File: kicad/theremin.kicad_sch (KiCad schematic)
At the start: 40 parts, among them J1 Eurorack Mono Jack, J2 Aerial, SW1 SW_SPDT, U1 4069, U2 4069, U3 LM386, U4 LP2950-5.0_TO92

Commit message: Updating with new footprints and some tweaks
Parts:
- removed D3: 1N4001, Diode_THT:D_DO-35_SOD27_P7.62mm_Horizontal, symbol Diode:1N4148
- removed H2: MountingHole_Pad, MountingHole:MountingHole_3.2mm_M3_DIN965_Pad, symbol Mechanical:MountingHole_Pad
- added D4: 1N4148, Diode_THT:D_DO-35_SOD27_P7.62mm_Horizontal, symbol Diode:1N4148
- added J3: Expression Attachment, Connector_PinHeader_2.54mm:PinHeader_1x02_P2.54mm_Vertical, symbol Connector:Conn_01x02_Pin
- added R12: 270k, Resistor_THT:R_Axial_DIN0207_L6.3mm_D2.5mm_P10.16mm_Horizontal, symbol Device:R
- BT1: footprint Connector_PinHeader_2.54mm:PinHeader_1x02_P2.54mm_Vertical -> Battery:BatteryHolder_Eagle_12BH611-GR
- C1, C2: footprint Rumblesan_Standard_Parts:C_Rect_L7.0mm_W3.5mm_P5.00mm -> Capacitor_THT:C_Rect_L7.0mm_W3.5mm_P5.00mm; Spec (none) -> ceramic C0G; Tolerance (none) -> 1%
- C10, C11, C6, C8, C9: footprint Rumblesan_Standard_Parts:CP_Radial_D5.0mm_P2.00mm -> Capacitor_THT:CP_Radial_D5.0mm_P2.50mm; symbol Rumblesan Standard Parts:C_Polarized -> Device:C_Polarized
- C12: footprint Rumblesan_Standard_Parts:C_Rect_L7.0mm_W3.5mm_P5.00mm -> Capacitor_THT:C_Rect_L7.0mm_W3.5mm_P5.00mm; symbol Rumblesan Standard Parts:C -> Device:C; Spec ceramic C0G -> ceramic X7R
- C3, C4, C5, C7: footprint Rumblesan_Standard_Parts:C_Rect_L7.0mm_W3.5mm_P5.00mm -> Capacitor_THT:C_Rect_L7.0mm_W3.5mm_P5.00mm; symbol Rumblesan Standard Parts:C -> Device:C
- H1: footprint MountingHole:MountingHole_3.2mm_M3_DIN965_Pad -> project-footprints:BCM_Logo_small_Copper_Pad_15mmx15mm; now left out of the parts list
- J2: now left out of the parts list
- LS1: footprint Connector_PinHeader_2.54mm:PinHeader_1x02_P2.54mm_Vertical -> project-footprints:Speaker_PUIAudio_AS04008MR-21-R
- R1, R10, R11, R2, R3, R4, R5, R6, R7, R8, R9: footprint Rumblesan_Standard_Parts:R_Axial_DIN0207_L6.3mm_D2.5mm_P10.16mm_Horizontal -> Resistor_THT:R_Axial_DIN0207_L6.3mm_D2.5mm_P10.16mm_Horizontal; symbol Rumblesan Standard Parts:R -> Device:R
- RV2: value 100k -> 25k; footprint Rumblesan_Standard_Parts:Potentiometer_Alpha_RD901F-40-00D_Single_Vertical -> Potentiometer_THT:Potentiometer_Alpha_RD901F-40-00D_Single_Vertical
- RV3: footprint Rumblesan_Standard_Parts:Potentiometer_Alpha_RD901F-40-00D_Single_Vertical -> Potentiometer_THT:Potentiometer_Alpha_RD901F-40-00D_Single_Vertical
- SW1: footprint Rumblesan_Standard_Parts:SW_SPDT_DailyWell_Sub_MiniToggle -> Button_Switch_THT:SW_CuK_OS102011MA1QN1_SPDT_Angled; MPRN (none) -> OS102011MA1QN1
- U1, U2: footprint Rumblesan_Standard_Parts:DIP-14_W7.62mm_Socket -> Package_DIP:DIP-14_W7.62mm_Socket_LongPads
- U3: footprint Rumblesan_Standard_Parts:DIP-8_W7.62mm_Socket -> Package_DIP:DIP-8_W7.62mm_Socket_LongPads
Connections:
- net GND: now also R11.1, R5.1, R9.1, D4.2 (A), R12.1; no longer R11.2, R5.2, R9.2
- net SPEAKER_AMP: now also R12.2
- net at U1.1: now also R1.1; no longer R1.2
- net at U1.2, U1.3: now also R2.1; no longer R2.2
- net at C5.2, U1.11, U1.13: now also R7.2, R8.2; no longer R7.1, R8.1
- net at U2.10, U2.9: now also C2.1; no longer C2.2
- net at R6.2: now also C4.2, R7.1; no longer C3.2
- net at U2.11, U2.12: now also R4.1; no longer R4.2
- net at U2.13: now also R3.1; no longer R3.2
- net at D1.1 (K), D2.1 (K), U1.9: now also R5.2; no longer R5.1
- net at J1.2 (Tip), RV2.2: now also J3.1 (Pin_1)
- net at U1.4, U1.5: now also C1.1; no longer C1.2
- net at C5.1, C6.1, U1.10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: now also R8.1; no longer R8.2
- net at RV3.3: now also R11.2; no longer R11.1
- net at C11.1, U4.3 (VI): now also R10.2, D4.1 (K); no longer R10.1
- net at RV1.2, RV1.3: now also R4.2; no longer R4.1
- net at C6.2, RV2.1: now also J3.2 (Pin_2)
- net at C7.1: now also R9.2; no longer R9.1
- net at SW1.1 (A): now also R10.1; no longer R10.2
- new net: C1.2, J2.1 (Pin_1), J2.2 (Pin_2), R1.2, R2.2
- new net: C3.2, R6.1
- new net: C2.2, R3.2, RV1.1
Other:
- note added: "BCM Logo with Ground Connection"
- moved on the sheet: BT1, C10, C11, C12, C5, C6, C7, C8, C9, J1, LS1, R10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

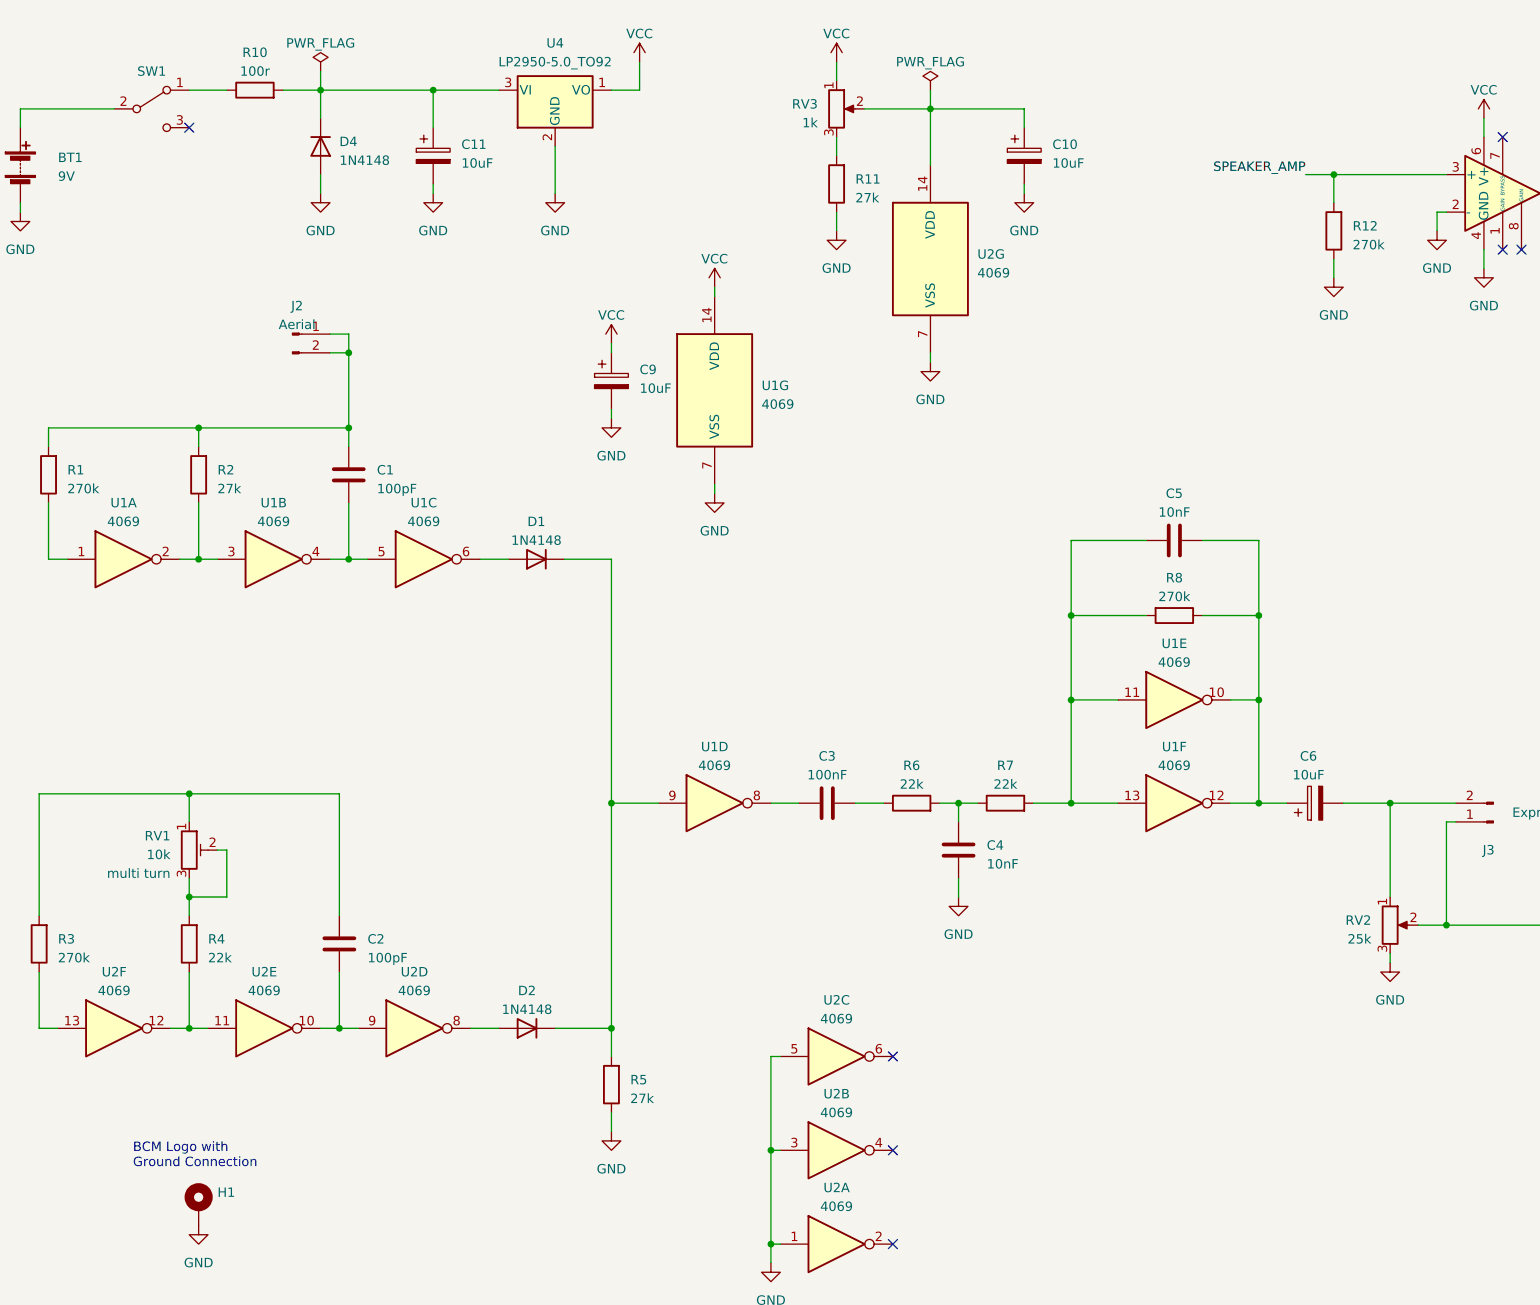
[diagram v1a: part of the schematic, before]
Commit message: Now with extra pretty!
Added the updated prettiefied version of the theremin files and added some quality of life features such as battery clip, crocodile clip friendly connectors, built in speaker & a power switch
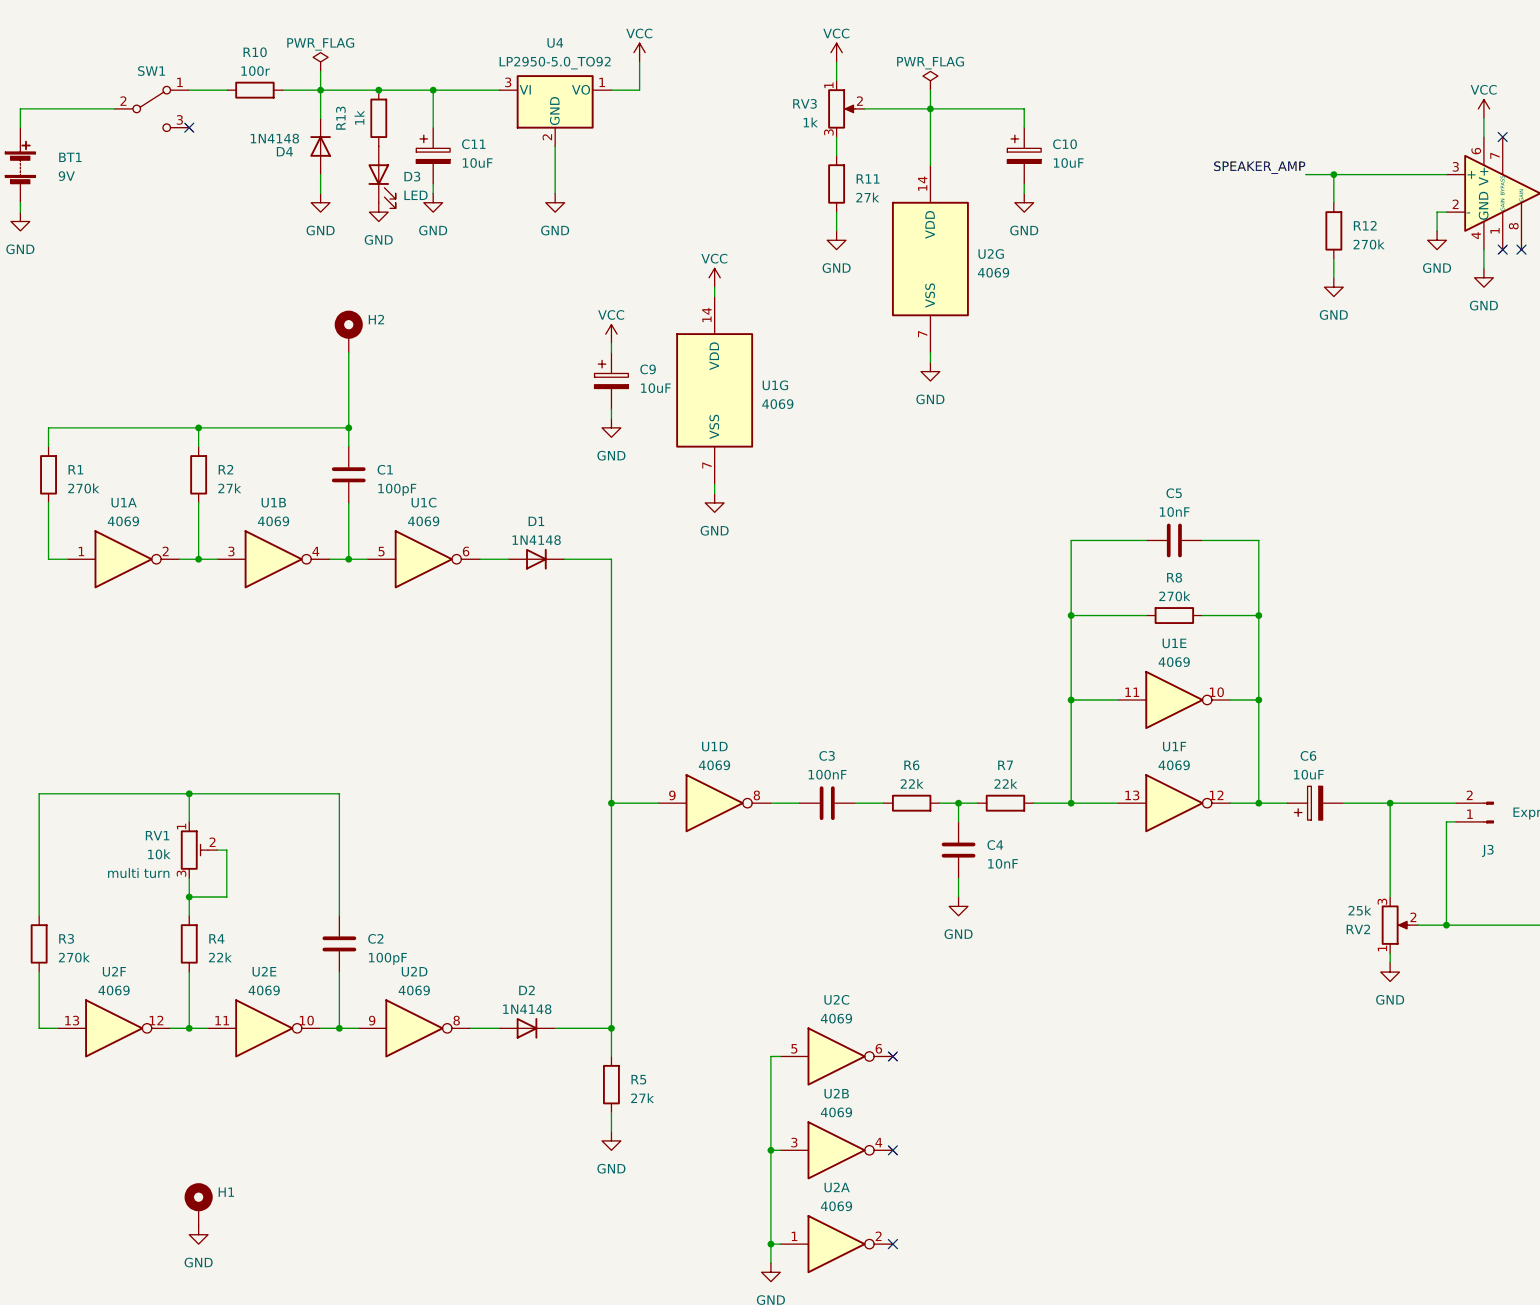
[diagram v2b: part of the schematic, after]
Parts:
- removed J2: Aerial, Connector_PinHeader_2.54mm:PinHeader_1x02_P2.54mm_Vertical, symbol Connector:Conn_01x02_Pin
- added D3: LED, LED_THT:LED_D5.0mm, symbol Device:LED
- added H2: MountingHole_Pad, TestPoint:crocclipcircleee, symbol Mechanical:MountingHole_Pad
- added R13: 1k, Resistor_THT:R_Axial_DIN0207_L6.3mm_D2.5mm_P10.16mm_Horizontal, symbol Device:R
- BT1: footprint Battery:BatteryHolder_Eagle_12BH611-GR -> Battery:BatteryHolder_Eagle_12BH611-GRMODDEDBYROBIN
- H1: footprint project-footprints:BCM_Logo_small_Copper_Pad_15mmx15mm -> TestPoint:crocclipcircleee
- LS1: footprint project-footprints:Speaker_PUIAudio_AS04008MR-21-R -> Librarythawney:40mmSpeakerdropin
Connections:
- net GND: now also RV2.1, D3.1 (K); no longer RV2.3
- net at C1.2, R1.2, R2.2: now also H2.1
- net at C11.1, D4.1 (K), R10.2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: now also R13.2
- net at C6.2, J3.2 (Pin_2): now also RV2.3; no longer RV2.1
- new net: D3.2 (A), R13.1
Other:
- note removed: "BCM Logo with Ground Connection"

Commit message: Tidying things up a bit
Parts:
- H1, H2: footprint TestPoint:crocclipcircleee -> project-footprints:crocclipcircleee
- J1: footprint Rumblesan_Standard_Parts:Jack_3.5mm_QingPu_WQP-PJ398SM_Vertical -> Rumblesan_Audio_Connectors:Jack_3.5mm_QingPu_WQP-PJ398SM_Vertical; symbol Audio_Connectors:Eurorack_Mono_Jack -> Connector_Audio:AudioJack2_SwitchT
- LS1: footprint Librarythawney:40mmSpeakerdropin -> project-footprints:40mmSpeakerdropin
- RV1: symbol Rumblesan Standard Parts:R_Potentiometer_Trim -> Standard_Parts:R_Potentiometer_Trim; Spec multi turn -> single turn
- RV2, RV3: symbol Rumblesan Standard Parts:R_Potentiometer -> Device:R_Potentiometer
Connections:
- net GND: now also J1.S; no longer J1.1 (Sleeve)
- net SPEAKER_AMP: now also J1.TN; no longer J1.3 (Tip_normalize)
- net at J3.1 (Pin_1), RV2.2: now also J1.T; no longer J1.2 (Tip)
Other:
- moved on the sheet: D3, D4, J1, R13

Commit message: More updates
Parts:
- RV1: footprint Rumblesan_Standard_Parts:Potentiometer_THT_Bourns_3306P_Vertical -> project-footprints:Potentiometer_THT_Bourns_3306P_Vertical
- SW1: footprint Button_Switch_THT:SW_CuK_OS102011MA1QN1_SPDT_Angled -> Button_Switch_THT:SW_Slide_SPDT_Angled_CK_OS102011MA1Q
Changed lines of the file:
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@@
 			)
 		)
-		(property "Footprint" "Rumblesan_Standard_Parts:Potentiometer_THT_Bourns_3306P_Vertical"
+		(property "Footprint" "project-footprints:Potentiometer_THT_Bourns_3306P_Vertical"
 			(at 36.83 133.35 90)
 			(effects
@@
 			)
 		)
-		(property "Footprint" "Button_Switch_THT:SW_CuK_OS102011MA1QN1_SPDT_Angled"
+		(property "Footprint" "Button_Switch_THT:SW_Slide_SPDT_Angled_CK_OS102011MA1Q"
 			(at 43.18 31.75 0)
 			(effects

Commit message: More tweaks
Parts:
- BT1: footprint Battery:BatteryHolder_Eagle_12BH611-GRMODDEDBYROBIN -> project-footprints:BatteryHolder_Eagle_12BH611-GRMODDEDBYROBIN
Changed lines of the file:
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@@
 			)
 		)
-		(property "Footprint" "Battery:BatteryHolder_Eagle_12BH611-GRMODDEDBYROBIN"
+		(property "Footprint" "project-footprints:BatteryHolder_Eagle_12BH611-GRMODDEDBYROBIN"
 			(at 25.4 37.846 90)
 			(effects

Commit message: Fixing issues with layout
* Making sure speaker fixing copper isn't covered on speaker footprint
* Adding two more plated holes to make fixing speaker easier
* Making holes for battery holder smaller so easier to solder
* Adding another mounting hole for faceplate
* Tweaking value and reference text placements
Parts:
- RV1: footprint project-footprints:Potentiometer_THT_Bourns_3306P_Vertical -> Rumblesan_Potentiometer_THT:Potentiometer_THT_Bourns_3306P_Vertical
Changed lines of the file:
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@@
 			)
 		)
-		(property "Footprint" "project-footprints:Potentiometer_THT_Bourns_3306P_Vertical"
+		(property "Footprint" "Rumblesan_Potentiometer_THT:Potentiometer_THT_Bourns_3306P_Vertical"
 			(at 36.83 133.35 90)
 			(effects

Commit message: Adding schematic page text
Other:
- company: (none) -> Bristol Communal Modular
- title: (none) -> Clara
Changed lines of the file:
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@@
 	(paper "A4")
 	(title_block
+		(title "Clara")
+		(date "2024-09-18")
+		(rev "rev2")
+		(company "Bristol Communal Modular")
 		(comment 2 "creativecommons.org/licenses/by/4.0/")
 		(comment 3 "License: CC BY 4.0")
